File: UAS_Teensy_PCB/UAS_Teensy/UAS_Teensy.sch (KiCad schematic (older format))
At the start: 8 parts

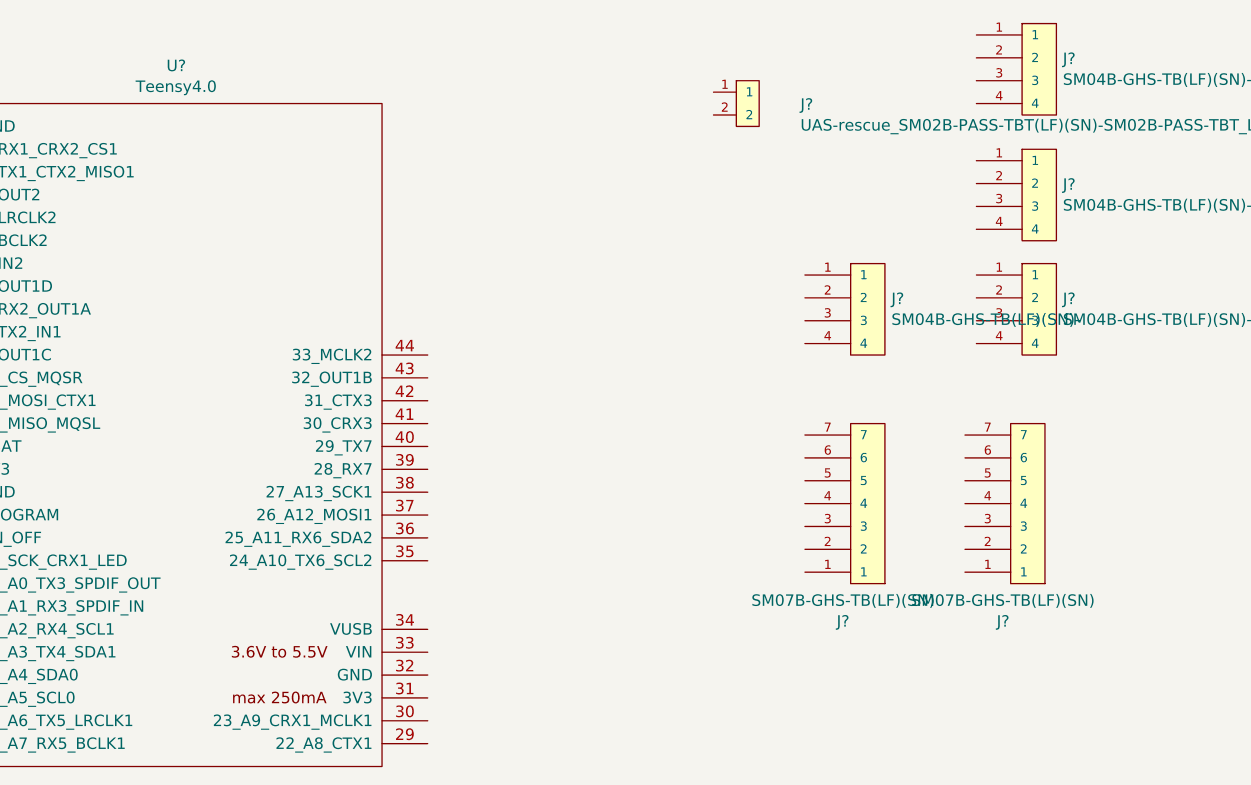
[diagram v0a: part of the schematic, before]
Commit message: Teensy Board Prep V1.1
Updated the Teensy Footprint/Symbol to match. Added entire Teensy library in case we just decided to use a Teensy 1.0 #businessMindset
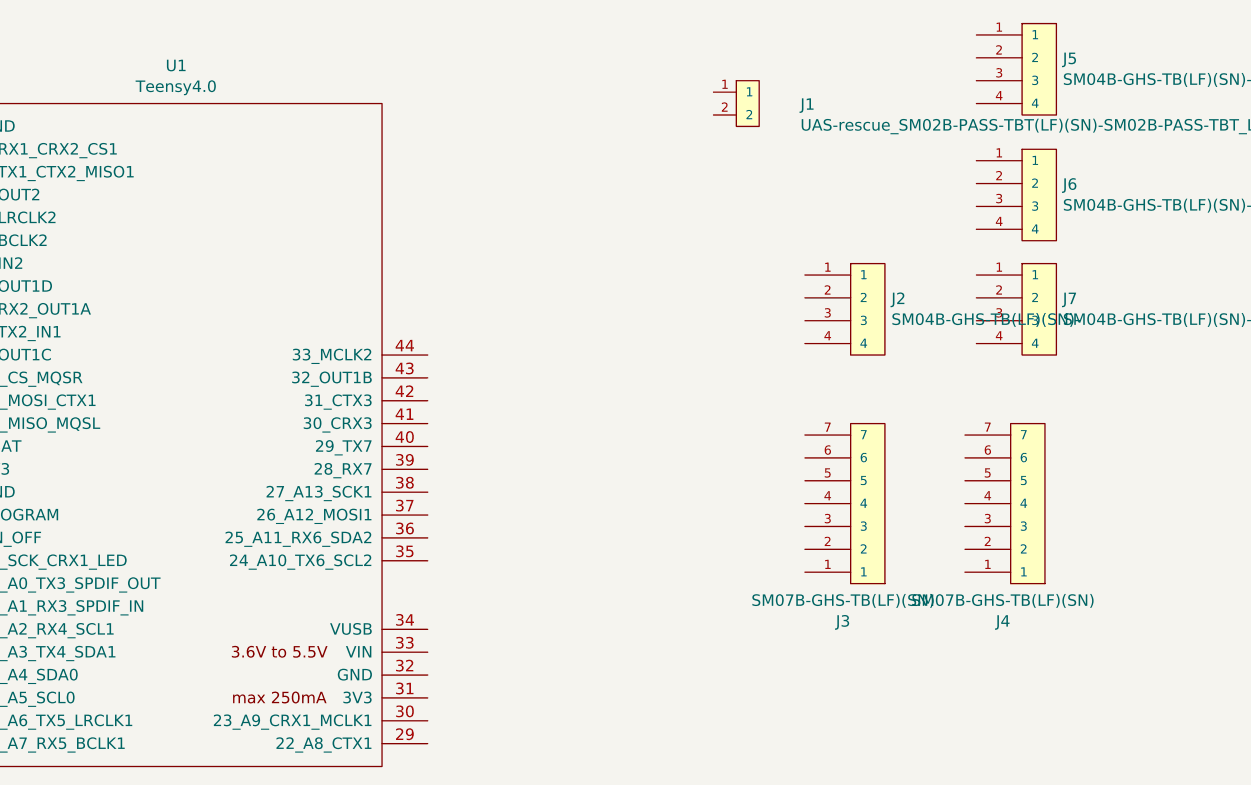
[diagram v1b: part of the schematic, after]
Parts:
- U1: renamed from U?; footprint (none) -> UAS_Teensy:Teensy40
- gave numbers to parts that had none: 7
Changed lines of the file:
@@
 $EndDescr
 $Comp
-L UAS_Teensy:Teensy4.0 U?
+L UAS_Teensy:Teensy4.0 U1
 U 1 1 6073EB87
 P 5250 2750
-F 0 "U?" H 5250 4365 50  0000 C CNN
+F 0 "U1" H 5250 4365 50  0000 C CNN
 F 1 "Teensy4.0" H 5250 4274 50  0000 C CNN
-F 2 "" H 4850 2950 50  0001 C CNN
+F 2 "UAS_Teensy:Teensy40" H 4850 2950 50  0001 C CNN
 F 3 "" H 4850 2950 50  0001 C CNN
 	1    5250 2750
@@
 $EndComp
 $Comp
-L UAS:SM04B-GHS-TB(LF)(SN)- J?
+L UAS:SM04B-GHS-TB(LF)(SN)- J2
 U 1 1 6073EDF2
 P 8400 2250
-F 0 "J?" H 8378 2346 50  0000 L CNN
+F 0 "J2" H 8378 2346 50  0000 L CNN
 F 1 "SM04B-GHS-TB(LF)(SN)-" H 8378 2255 50  0000 L CNN
 F 2 "JST_SM04B-GHS-TB(LF)(SN)-" H 8400 2250 50  0001 L BNN
@@
 $EndComp
 $Comp
-L UAS:SM07B-GHS-TB(LF)(SN) J?
+L UAS:SM07B-GHS-TB(LF)(SN) J3
 U 1 1 6073F50A
 P 8400 2950
-F 0 "J?" H 8633 3565 50  0000 C CNN
+F 0 "J3" H 8633 3565 50  0000 C CNN
 F 1 "SM07B-GHS-TB(LF)(SN)" H 8633 3474 50  0000 C CNN
 F 2 "JST_SM07B-GHS-TB(LF)(SN)" H 8400 2950 50  0001 L BNN
@@
 $EndComp
 $Comp
-L UAS:SM07B-GHS-TB(LF)(SN) J?
+L UAS:SM07B-GHS-TB(LF)(SN) J4
 U 1 1 60740985
 P 9100 2950
-F 0 "J?" H 9333 3565 50  0000 C CNN
+F 0 "J4" H 9333 3565 50  0000 C CNN
 F 1 "SM07B-GHS-TB(LF)(SN)" H 9333 3474 50  0000 C CNN
 F 2 "JST_SM07B-GHS-TB(LF)(SN)" H 9100 2950 50  0001 L BNN
@@
 $EndComp
 $Comp
-L UAS:SM04B-GHS-TB(LF)(SN)- J?
+L UAS:SM04B-GHS-TB(LF)(SN)- J5
 U 1 1 60740F72
 P 9150 1200
-F 0 "J?" H 9128 1296 50  0000 L CNN
+F 0 "J5" H 9128 1296 50  0000 L CNN
 F 1 "SM04B-GHS-TB(LF)(SN)-" H 9128 1205 50  0000 L CNN
 F 2 "JST_SM04B-GHS-TB(LF)(SN)-" H 9150 1200 50  0001 L BNN
@@
 $EndComp
 $Comp
-L UAS:SM04B-GHS-TB(LF)(SN)- J?
+L UAS:SM04B-GHS-TB(LF)(SN)- J6
 U 1 1 60741E63
 P 9150 1750
-F 0 "J?" H 9128 1846 50  0000 L CNN
+F 0 "J6" H 9128 1846 50  0000 L CNN
 F 1 "SM04B-GHS-TB(LF)(SN)-" H 9128 1755 50  0000 L CNN
 F 2 "JST_SM04B-GHS-TB(LF)(SN)-" H 9150 1750 50  0001 L BNN
@@
 $EndComp
 $Comp
-L UAS:SM04B-GHS-TB(LF)(SN)- J?
+L UAS:SM04B-GHS-TB(LF)(SN)- J7
 U 1 1 60742445
 P 9150 2250
-F 0 "J?" H 9128 2346 50  0000 L CNN
+F 0 "J7" H 9128 2346 50  0000 L CNN
 F 1 "SM04B-GHS-TB(LF)(SN)-" H 9128 2255 50  0000 L CNN
 F 2 "JST_SM04B-GHS-TB(LF)(SN)-" H 9150 2250 50  0001 L BNN
@@
 $EndComp
 $Comp
-L UAS:UAS-rescue_SM02B-PASS-TBT(LF)(SN)-SM02B-PASS-TBT_LF__SN_ J?
+L UAS:UAS-rescue_SM02B-PASS-TBT(LF)(SN)-SM02B-PASS-TBT_LF__SN_ J1
 U 1 1 60742753
 P 7750 1300
-F 0 "J?" H 7980 1296 50  0000 L CNN
+F 0 "J1" H 7980 1296 50  0000 L CNN
 F 1 "UAS-rescue_SM02B-PASS-TBT(LF)(SN)-SM02B-PASS-TBT_LF__SN_" H 7980 1205 50  0000 L CNN
 F 2 "JST_SM02B-PASS-TBT(LF)(SN)" H 7750 1300 50  0001 L BNN

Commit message: Schematic Wiring V1
First Step in Schematic Wiring
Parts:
- added U2: BNO055, UAS_Teensy:BNO055_Breakout, symbol UAS_Teensy:BNO055
- J1: footprint JST_SM02B-PASS-TBT(LF)(SN) -> UAS_Teensy:SM02BGHSTBLFSN
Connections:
- net at U1.1 (GND): now also J3.1, J4.1
- net at U1.10 (8_TX2_IN1): now also J4.4
- net at U1.11 (9_OUT1C): now also J4.5
- net at U1.12 (10_CS_MQSR): now also J4.6
- net at U1.13 (11_MOSI_CTX1): now also J4.7
- net at U1.18 (PROGRAM): now also J1.1
- net at U1.19 (ON_OFF): now also J1.2
- net at U1.2 (0_RX1_CRX2_CS1): now also J3.2
- net at U1.3 (1_TX1_CTX2_MISO1): now also J3.3
- net at U1.4 (2_OUT2): now also J3.4
- net at U1.5 (3_LRCLK2): now also J3.5
- net at U1.6 (4_BCLK2): now also J3.6
- net at U1.7 (5_IN2): now also J3.7
- net at U1.8 (6_OUT1D): now also J4.2
- net at U1.9 (7_RX2_OUT1A): now also J4.3
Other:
- moved on the sheet: J1, J2, J3, J4, J5, J6, J7
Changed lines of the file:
@@
 L UAS:SM04B-GHS-TB(LF)(SN)- J2
 U 1 1 6073EDF2
-P 8400 2250
-F 0 "J2" H 8378 2346 50  0000 L CNN
-F 1 "SM04B-GHS-TB(LF)(SN)-" H 8378 2255 50  0000 L CNN
-F 2 "JST_SM04B-GHS-TB(LF)(SN)-" H 8400 2250 50  0001 L BNN
-F 3 "" H 8400 2250 50  0001 L BNN
-F 4 "NA" H 8400 2250 50  0001 L BNN "PARTREV"
-F 5 "Manufacturer Recommendations" H 8400 2250 50  0001 L BNN "STANDARD"
-F 6 "JHS" H 8400 2250 50  0001 L BNN "MANUFACTURER"
-	1    8400 2250
+P 7150 2600
+F 0 "J2" H 7128 2696 50  0000 L CNN
+F 1 "SM04B-GHS-TB(LF)(SN)-" H 7128 2605 50  0000 L CNN
+F 2 "JST_SM04B-GHS-TB(LF)(SN)-" H 7150 2600 50  0001 L BNN
+F 3 "" H 7150 2600 50  0001 L BNN
+F 4 "NA" H 7150 2600 50  0001 L BNN "PARTREV"
+F 5 "Manufacturer Recommendations" H 7150 2600 50  0001 L BNN "STANDARD"
+F 6 "JHS" H 7150 2600 50  0001 L BNN "MANUFACTURER"
+	1    7150 2600
 	1    0    0    -1
 $EndComp
@@
 L UAS:SM07B-GHS-TB(LF)(SN) J3
 U 1 1 6073F50A
-P 8400 2950
-F 0 "J3" H 8633 3565 50  0000 C CNN
-F 1 "SM07B-GHS-TB(LF)(SN)" H 8633 3474 50  0000 C CNN
-F 2 "JST_SM07B-GHS-TB(LF)(SN)" H 8400 2950 50  0001 L BNN
-F 3 "" H 8400 2950 50  0001 L BNN
-F 4 "MANUFACTURER STANDARD" H 8400 2950 50  0001 L BNN "STANDARD"
-F 5 "JST" H 8400 2950 50  0001 L BNN "MANUFACTURER"
-F 6 "NA" H 8400 2950 50  0001 L BNN "PARTREV"
-	1    8400 2950
-	-1   0    0    1
+P 3500 1800
+F 0 "J3" H 3733 2415 50  0000 C CNN
+F 1 "SM07B-GHS-TB(LF)(SN)" H 3733 2324 50  0000 C CNN
+F 2 "JST_SM07B-GHS-TB(LF)(SN)" H 3500 1800 50  0001 L BNN
+F 3 "" H 3500 1800 50  0001 L BNN
+F 4 "MANUFACTURER STANDARD" H 3500 1800 50  0001 L BNN "STANDARD"
+F 5 "JST" H 3500 1800 50  0001 L BNN "MANUFACTURER"
+F 6 "NA" H 3500 1800 50  0001 L BNN "PARTREV"
+	1    3500 1800
+	1    0    0    -1
 $EndComp
 $Comp
 L UAS:SM07B-GHS-TB(LF)(SN) J4
 U 1 1 60740985
-P 9100 2950
-F 0 "J4" H 9333 3565 50  0000 C CNN
-F 1 "SM07B-GHS-TB(LF)(SN)" H 9333 3474 50  0000 C CNN
-F 2 "JST_SM07B-GHS-TB(LF)(SN)" H 9100 2950 50  0001 L BNN
-F 3 "" H 9100 2950 50  0001 L BNN
-F 4 "MANUFACTURER STANDARD" H 9100 2950 50  0001 L BNN "STANDARD"
-F 5 "JST" H 9100 2950 50  0001 L BNN "MANUFACTURER"
-F 6 "NA" H 9100 2950 50  0001 L BNN "PARTREV"
-	1    9100 2950
-	-1   0    0    1
+P 3300 2600
+F 0 "J4" H 3533 3215 50  0000 C CNN
+F 1 "SM07B-GHS-TB(LF)(SN)" H 3533 3124 50  0000 C CNN
+F 2 "JST_SM07B-GHS-TB(LF)(SN)" H 3300 2600 50  0001 L BNN
+F 3 "" H 3300 2600 50  0001 L BNN
+F 4 "MANUFACTURER STANDARD" H 3300 2600 50  0001 L BNN "STANDARD"
+F 5 "JST" H 3300 2600 50  0001 L BNN "MANUFACTURER"
+F 6 "NA" H 3300 2600 50  0001 L BNN "PARTREV"
+	1    3300 2600
+	1    0    0    -1
 $EndComp
 $Comp
 L UAS:SM04B-GHS-TB(LF)(SN)- J5
 U 1 1 60740F72
-P 9150 1200
-F 0 "J5" H 9128 1296 50  0000 L CNN
-F 1 "SM04B-GHS-TB(LF)(SN)-" H 9128 1205 50  0000 L CNN
-F 2 "JST_SM04B-GHS-TB(LF)(SN)-" H 9150 1200 50  0001 L BNN
-F 3 "" H 9150 1200 50  0001 L BNN
-F 4 "NA" H 9150 1200 50  0001 L BNN "PARTREV"
-F 5 "Manufacturer Recommendations" H 9150 1200 50  0001 L BNN "STANDARD"
-F 6 "JHS" H 9150 1200 50  0001 L BNN "MANUFACTURER"
-	1    9150 1200
+P 7900 1550
+F 0 "J5" H 7878 1646 50  0000 L CNN
+F 1 "SM04B-GHS-TB(LF)(SN)-" H 7878 1555 50  0000 L CNN
+F 2 "JST_SM04B-GHS-TB(LF)(SN)-" H 7900 1550 50  0001 L BNN
+F 3 "" H 7900 1550 50  0001 L BNN
+F 4 "NA" H 7900 1550 50  0001 L BNN "PARTREV"
+F 5 "Manufacturer Recommendations" H 7900 1550 50  0001 L BNN "STANDARD"
+F 6 "JHS" H 7900 1550 50  0001 L BNN "MANUFACTURER"
+	1    7900 1550
 	1    0    0    -1
 $EndComp
@@
 L UAS:SM04B-GHS-TB(LF)(SN)- J6
 U 1 1 60741E63
-P 9150 1750
-F 0 "J6" H 9128 1846 50  0000 L CNN
-F 1 "SM04B-GHS-TB(LF)(SN)-" H 9128 1755 50  0000 L CNN
-F 2 "JST_SM04B-GHS-TB(LF)(SN)-" H 9150 1750 50  0001 L BNN
-F 3 "" H 9150 1750 50  0001 L BNN
-F 4 "NA" H 9150 1750 50  0001 L BNN "PARTREV"
-F 5 "Manufacturer Recommendations" H 9150 1750 50  0001 L BNN "STANDARD"
-F 6 "JHS" H 9150 1750 50  0001 L BNN "MANUFACTURER"
-	1    9150 1750
+P 7900 2100
+F 0 "J6" H 7878 2196 50  0000 L CNN
+F 1 "SM04B-GHS-TB(LF)(SN)-" H 7878 2105 50  0000 L CNN
+F 2 "JST_SM04B-GHS-TB(LF)(SN)-" H 7900 2100 50  0001 L BNN
+F 3 "" H 7900 2100 50  0001 L BNN
+F 4 "NA" H 7900 2100 50  0001 L BNN "PARTREV"
+F 5 "Manufacturer Recommendations" H 7900 2100 50  0001 L BNN "STANDARD"
+F 6 "JHS" H 7900 2100 50  0001 L BNN "MANUFACTURER"
+	1    7900 2100
 	1    0    0    -1
 $EndComp
@@
 L UAS:SM04B-GHS-TB(LF)(SN)- J7
 U 1 1 60742445
-P 9150 2250
-F 0 "J7" H 9128 2346 50  0000 L CNN
-F 1 "SM04B-GHS-TB(LF)(SN)-" H 9128 2255 50  0000 L CNN
-F 2 "JST_SM04B-GHS-TB(LF)(SN)-" H 9150 2250 50  0001 L BNN
-F 3 "" H 9150 2250 50  0001 L BNN
-F 4 "NA" H 9150 2250 50  0001 L BNN "PARTREV"
-F 5 "Manufacturer Recommendations" H 9150 2250 50  0001 L BNN "STANDARD"
-F 6 "JHS" H 9150 2250 50  0001 L BNN "MANUFACTURER"
-	1    9150 2250
+P 7900 2600
+F 0 "J7" H 7878 2696 50  0000 L CNN
+F 1 "SM04B-GHS-TB(LF)(SN)-" H 7878 2605 50  0000 L CNN
+F 2 "JST_SM04B-GHS-TB(LF)(SN)-" H 7900 2600 50  0001 L BNN
+F 3 "" H 7900 2600 50  0001 L BNN
+F 4 "NA" H 7900 2600 50  0001 L BNN "PARTREV"
+F 5 "Manufacturer Recommendations" H 7900 2600 50  0001 L BNN "STANDARD"
+F 6 "JHS" H 7900 2600 50  0001 L BNN "MANUFACTURER"
+	1    7900 2600
 	1    0    0    -1
 $EndComp
@@
 L UAS:UAS-rescue_SM02B-PASS-TBT(LF)(SN)-SM02B-PASS-TBT_LF__SN_ J1
 U 1 1 60742753
-P 7750 1300
-F 0 "J1" H 7980 1296 50  0000 L CNN
-F 1 "UAS-rescue_SM02B-PASS-TBT(LF)(SN)-SM02B-PASS-TBT_LF__SN_" H 7980 1205 50  0000 L CNN
-F 2 "JST_SM02B-PASS-TBT(LF)(SN)" H 7750 1300 50  0001 L BNN
-F 3 "" H 7750 1300 50  0001 L BNN
-F 4 "N/A" H 7750 1300 50  0001 L BNN "PARTREV"
-F 5 "JST" H 7750 1300 50  0001 L BNN "MANUFACTURER"
-F 6 "Manufacturer Recommendations" H 7750 1300 50  0001 L BNN "STANDARD"
-F 7 "5.7 mm" H 7750 1300 50  0001 L BNN "MAXIMUM_PACKAGE_HEIGHT"
-	1    7750 1300
+P 3850 3150
+F 0 "J1" H 4080 3146 50  0000 L CNN
+F 1 "UAS-rescue_SM02B-PASS-TBT(LF)(SN)-SM02B-PASS-TBT_LF__SN_" H 4080 3055 50  0000 L CNN
+F 2 "UAS_Teensy:SM02BGHSTBLFSN" H 3850 3150 50  0001 L BNN
+F 3 "" H 3850 3150 50  0001 L BNN
+F 4 "N/A" H 3850 3150 50  0001 L BNN "PARTREV"
+F 5 "JST" H 3850 3150 50  0001 L BNN "MANUFACTURER"
+F 6 "Manufacturer Recommendations" H 3850 3150 50  0001 L BNN "STANDARD"
+F 7 "5.7 mm" H 3850 3150 50  0001 L BNN "MAXIMUM_PACKAGE_HEIGHT"
+	1    3850 3150
+	-1   0    0    1
+$EndComp
+Wire Wire Line
+	3700 2200 3750 2200
+Wire Wire Line
+	3750 2200 3750 2100
+Wire Wire Line
+	3750 2100 3500 2100
+Wire Wire Line
+	3500 2100 3500 1300
+Wire Wire Line
+	3500 1300 4100 1300
+Wire Wire Line
+	4100 1300 4100 1400
+Wire Wire Line
+	4100 1400 4150 1400
+Wire Wire Line
+	3900 1400 4100 1400
+Connection ~ 4100 1400
+Wire Wire Line
+	3700 2300 3800 2300
+Wire Wire Line
+	3800 2300 3800 2100
+Wire Wire Line
+	3800 2100 4150 2100
+Wire Wire Line
+	3700 2400 3850 2400
+Wire Wire Line
+	3850 2400 3850 2200
+Wire Wire Line
+	3850 2200 4150 2200
+Wire Wire Line
+	4150 2300 3900 2300
+Wire Wire Line
+	3900 2300 3900 2500
+Wire Wire Line
+	3900 2500 3700 2500
+Wire Wire Line
+	4150 2400 3950 2400
+Wire Wire Line
+	3950 2400 3950 2600
+Wire Wire Line
+	3950 2600 3700 2600
+Wire Wire Line
+	3700 2700 4000 2700
+Wire Wire Line
+	4000 2700 4000 2500
+Wire Wire Line
+	4000 2500 4150 2500
+Wire Wire Line
+	3700 2800 4050 2800
+Wire Wire Line
+	4050 2800 4050 2600
+Wire Wire Line
+	4050 2600 4150 2600
+Wire Wire Line
+	4150 1500 3900 1500
+Wire Wire Line
+	3900 1600 4150 1600
+Wire Wire Line
+	4150 1700 3900 1700
+Wire Wire Line
+	3900 1800 4150 1800
+Wire Wire Line
+	4150 1900 3900 1900
+Wire Wire Line
+	3900 2000 4150 2000
+$Comp
+L UAS_Teensy:BNO055 U2
+U 1 1 6074FC0F
+P 6900 1800
+F 0 "U2" H 6875 2275 50  0000 C CNN
+F 1 "BNO055" H 6875 2184 50  0000 C CNN
+F 2 "UAS_Teensy:BNO055_Breakout" H 6900 2350 50  0001 C CNN
+F 3 "" H 6900 2350 50  0001 C CNN
+	1    6900 1800
 	1    0    0    -1
 $EndComp
+Wire Wire Line
+	4000 3100 4100 3100
+Wire Wire Line
+	4100 3100 4100 3200
+Wire Wire Line
+	4100 3200 4150 3200
+Wire Wire Line
+	4000 3200 4050 3200
+Wire Wire Line
+	4050 3200 4050 3150
+Wire Wire Line
+	4050 3150 4150 3150
+Wire Wire Line
+	4150 3150 4150 3100
 $EndSCHEMATC

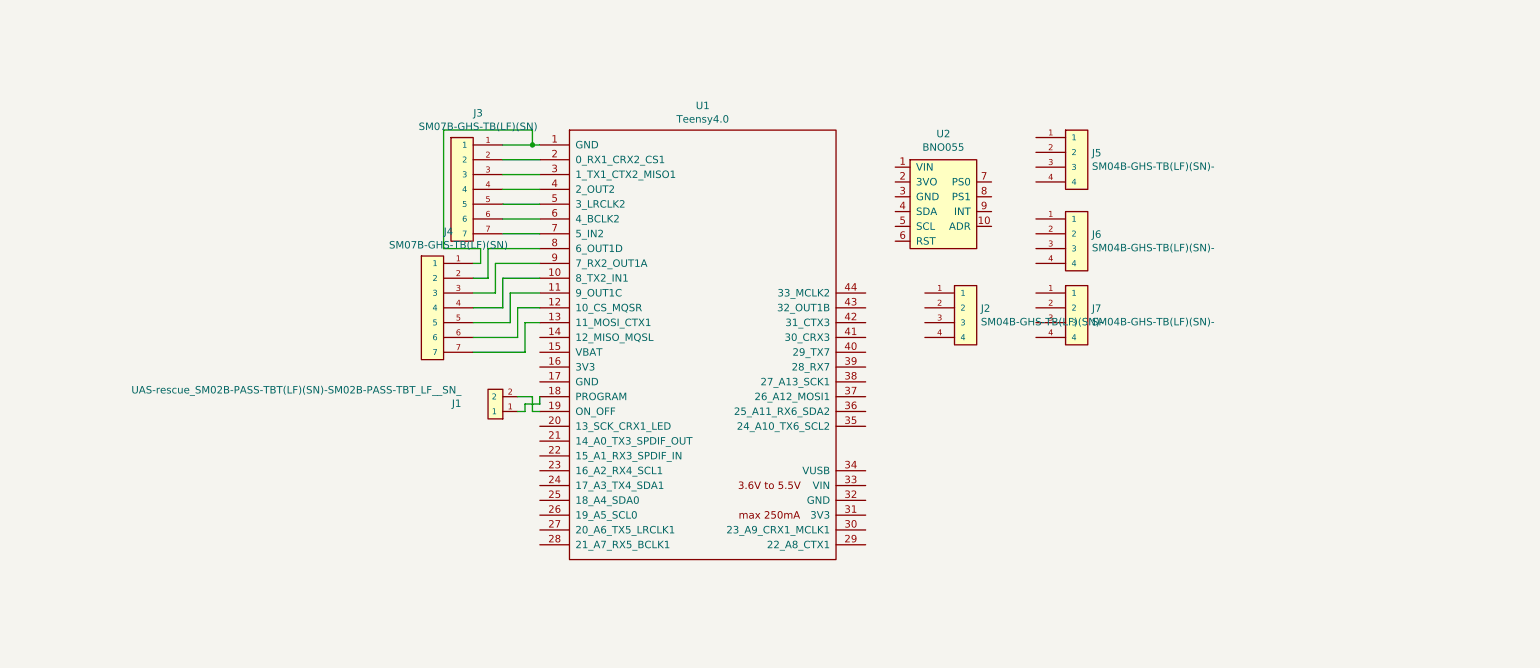
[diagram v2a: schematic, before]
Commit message: Teensy PCB Ready To Wire Up Update
Schematic is finalized and all that's left is to lay traces
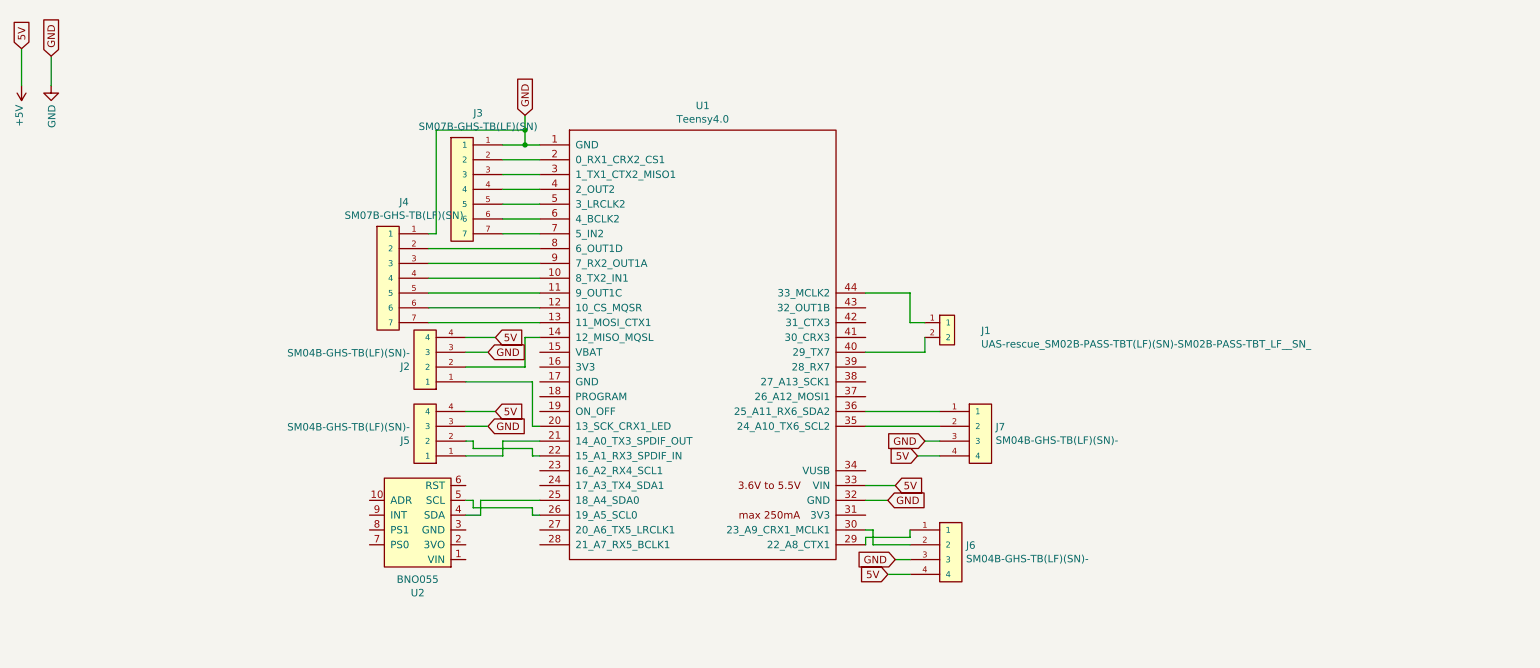
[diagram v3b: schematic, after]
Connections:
- net GND: now reaches J3.1, J4.1, U1.1 (GND)
- net GND: now also J2.3, J5.3, J6.3, J7.3, U1.32 (GND)
- net at U1.14 (12_MISO_MQSL): now also J2.2
- net at J1.1: now also U1.44 (33_MCLK2); no longer U1.18 (PROGRAM)
- net at J1.2: now also U1.40 (29_TX7); no longer U1.19 (ON_OFF)
- net at U1.20 (13_SCK_CRX1_LED): now also J2.1
- net at U1.21 (14_A0_TX3_SPDIF_OUT): now also J5.1
- net at U1.22 (15_A1_RX3_SPDIF_IN): now also J5.2
- net at U1.25 (18_A4_SDA0): now also U2.4 (SDA)
- net at U1.26 (19_A5_SCL0): now also U2.5 (SCL)
- net at U1.29 (22_A8_CTX1): now also J6.1
- net at U1.30 (23_A9_CRX1_MCLK1): now also J6.2
- net +5V: now reaches U1.33 (VIN)
- net +5V: now also J2.4, J5.4, J6.4, J7.4
- net at U1.35 (24_A10_TX6_SCL2): now also J7.2
- net at U1.36 (25_A11_RX6_SDA2): now also J7.1
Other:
- moved on the sheet: J1, J2, J4, J5, J6, J7, U2

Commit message: trace changes and fill for teensy pcb
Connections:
- net +5V: now also U2.1 (VIN)
- net GND: now also U2.3 (GND)
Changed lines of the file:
@@
 EESchema Schematic File Version 4
-LIBS:UAS_Teensy-cache
 EELAYER 30 0
 EELAYER END
@@
 5V
 Wire Wire Line
-	3650 3200 3850 3200
-Wire Wire Line
 	3650 3300 3800 3300
 Text GLabel 3800 3300 2    50   Input ~ 0
@@
 Wire Wire Line
 	4100 3900 4150 3900
+Wire Wire Line
+	3650 3200 3850 3200
+Text GLabel 3850 4200 2    50   Input ~ 0
+5V
+Wire Wire Line
+	3650 4200 3850 4200
+Wire Wire Line
+	3650 4000 3800 4000
+Text GLabel 3800 4000 2    50   Input ~ 0
+GND
 $EndSCHEMATC

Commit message: Teensy Board Updates
Teensy Board Updates
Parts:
- J3, J4: footprint JST_SM07B-GHS-TB(LF)(SN) -> UAS_Teensy:JST_SM08B-GHS-TB(LF)(SN)
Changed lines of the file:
@@
 EESchema Schematic File Version 4
+LIBS:UAS_Teensy-cache
 EELAYER 30 0
 EELAYER END
@@
 F 0 "J3" H 3733 2415 50  0000 C CNN
 F 1 "SM07B-GHS-TB(LF)(SN)" H 3733 2324 50  0000 C CNN
-F 2 "JST_SM07B-GHS-TB(LF)(SN)" H 3500 1800 50  0001 L BNN
+F 2 "UAS_Teensy:JST_SM08B-GHS-TB(LF)(SN)" H 3500 1800 50  0001 L BNN
 F 3 "" H 3500 1800 50  0001 L BNN
 F 4 "MANUFACTURER STANDARD" H 3500 1800 50  0001 L BNN "STANDARD"
@@
 F 0 "J4" H 3233 3015 50  0000 C CNN
 F 1 "SM07B-GHS-TB(LF)(SN)" H 3233 2924 50  0000 C CNN
-F 2 "JST_SM07B-GHS-TB(LF)(SN)" H 3000 2400 50  0001 L BNN
+F 2 "UAS_Teensy:JST_SM08B-GHS-TB(LF)(SN)" H 3000 2400 50  0001 L BNN
 F 3 "" H 3000 2400 50  0001 L BNN
 F 4 "MANUFACTURER STANDARD" H 3000 2400 50  0001 L BNN "STANDARD"
